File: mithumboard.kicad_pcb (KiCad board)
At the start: 2 copper layers, 28 parts, among them J1 AudioJack4, J2 AudioJack4, J3 AudioJack4, J4 AudioJack4, SW1 SW_Push, SW10 SW_Push, SW11 SW_Push, SW12 SW_Push, SW13 SW_Push, SW14 SW_Push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

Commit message: キースイッチのピン割り当て見直し
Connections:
- U1 pad 10: R2C2 -> R1C1
- U1 pad 11: R2C3 -> R1C2
- U1 pad 13: R2C4 -> R1C3
- U1 pad 14: R2C5 -> R1C4
- U1 pad 15: R3C1 -> R1C5
- U1 pad 16: R3C2 -> R2C4
- U1 pad 17: R3C3 -> R2C5
- U1 pad 18: R3C4 -> R3C5
- U1 pad 19: R3C5 -> R3C4
- U1 pad 4: R1C1 -> R3C3
- U1 pad 5: R1C2 -> R3C2
- U1 pad 6: R1C3 -> R3C1
- U1 pad 7: R1C4 -> R2C1
- U1 pad 8: R1C5 -> R2C3
- U1 pad 9: R2C1 -> R2C2
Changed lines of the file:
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@@
       (net 26 "Net-(U1-Pad20)"))
     (pad 19 smd rect (at 2.85 0.325) (size 1.1 0.4) (layers B.Cu B.Paste B.Mask)
+      (net 22 R3C4))
+    (pad 18 smd rect (at 2.85 -0.325) (size 1.1 0.4) (layers B.Cu B.Paste B.Mask)
       (net 23 R3C5))
-    (pad 18 smd rect (at 2.85 -0.325) (size 1.1 0.4) (layers B.Cu B.Paste B.Mask)
-      (net 22 R3C4))
     (pad 17 smd rect (at 2.85 -0.975) (size 1.1 0.4) (layers B.Cu B.Paste B.Mask)
-      (net 21 R3C3))
+      (net 18 R2C5))
     (pad 16 smd rect (at 2.85 -1.625) (size 1.1 0.4) (layers B.Cu B.Paste B.Mask)
-      (net 20 R3C2))
+      (net 17 R2C4))
     (pad 15 smd rect (at 2.85 -2.275) (size 1.1 0.4) (layers B.Cu B.Paste B.Mask)
-      (net 19 R3C1))
+      (net 13 R1C5))
     (pad 14 smd rect (at 2.85 -2.925) (size 1.1 0.4) (layers B.Cu B.Paste B.Mask)
-      (net 18 R2C5))
+      (net 12 R1C4))
     (pad 13 smd rect (at 2.85 -3.575) (size 1.1 0.4) (layers B.Cu B.Paste B.Mask)
-      (net 17 R2C4))
+      (net 11 R1C3))
     (pad 12 smd rect (at -2.85 -3.575) (size 1.1 0.4) (layers B.Cu B.Paste B.Mask)
       (net 1 GND))
     (pad 11 smd rect (at -2.85 -2.925) (size 1.1 0.4) (layers B.Cu B.Paste B.Mask)
+      (net 10 R1C2))
+    (pad 10 smd rect (at -2.85 -2.275) (size 1.1 0.4) (layers B.Cu B.Paste B.Mask)
+      (net 9 R1C1))
+    (pad 9 smd rect (at -2.85 -1.625) (size 1.1 0.4) (layers B.Cu B.Paste B.Mask)
+      (net 15 R2C2))
+    (pad 8 smd rect (at -2.85 -0.975) (size 1.1 0.4) (layers B.Cu B.Paste B.Mask)
       (net 16 R2C3))
-    (pad 10 smd rect (at -2.85 -2.275) (size 1.1 0.4) (layers B.Cu B.Paste B.Mask)
-      (net 15 R2C2))
-    (pad 9 smd rect (at -2.85 -1.625) (size 1.1 0.4) (layers B.Cu B.Paste B.Mask)
+    (pad 7 smd rect (at -2.85 -0.325) (size 1.1 0.4) (layers B.Cu B.Paste B.Mask)
       (net 14 R2C1))
-    (pad 8 smd rect (at -2.85 -0.975) (size 1.1 0.4) (layers B.Cu B.Paste B.Mask)
-      (net 13 R1C5))
-    (pad 7 smd rect (at -2.85 -0.325) (size 1.1 0.4) (layers B.Cu B.Paste B.Mask)
-      (net 12 R1C4))
     (pad 6 smd rect (at -2.85 0.325) (size 1.1 0.4) (layers B.Cu B.Paste B.Mask)
-      (net 11 R1C3))
+      (net 19 R3C1))
     (pad 5 smd rect (at -2.85 0.975) (size 1.1 0.4) (layers B.Cu B.Paste B.Mask)
-      (net 10 R1C2))
+      (net 20 R3C2))
     (pad 4 smd rect (at -2.85 1.625) (size 1.1 0.4) (layers B.Cu B.Paste B.Mask)
-      (net 9 R1C1))
+      (net 21 R3C3))
     (pad 3 smd rect (at -2.85 2.275) (size 1.1 0.4) (layers B.Cu B.Paste B.Mask)
       (net 8 A2))

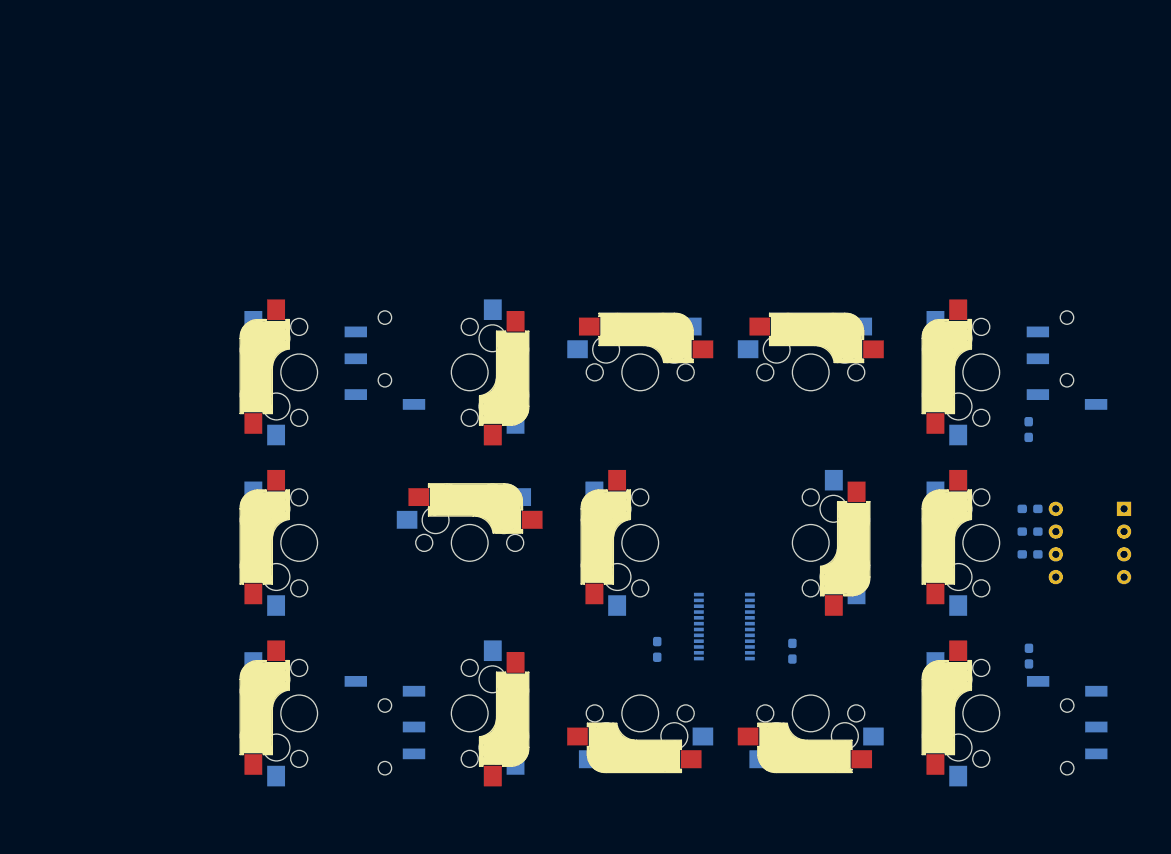
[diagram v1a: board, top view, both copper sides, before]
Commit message: 全部線引き終わり
ただし基板を180度回転させたので、キースイッチの行列のラベルを張りなおす必要あり。
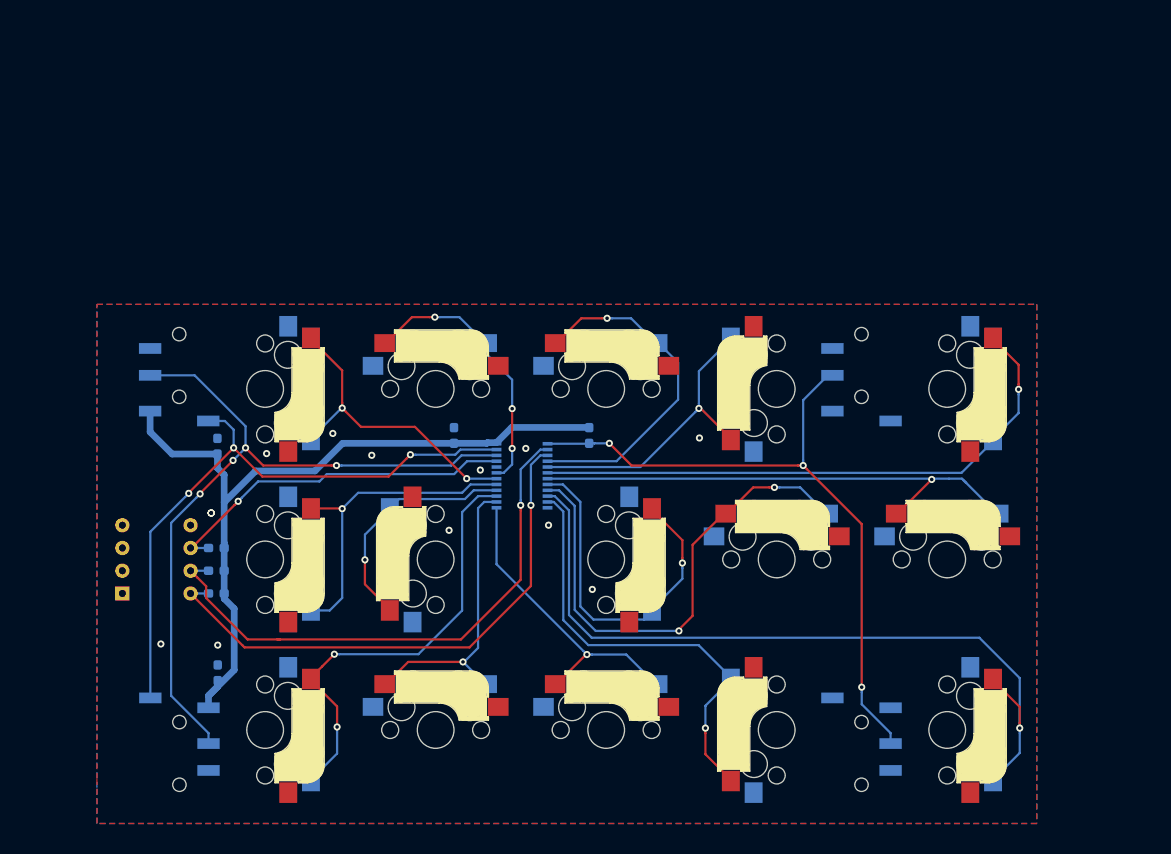
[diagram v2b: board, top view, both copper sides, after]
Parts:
- moved SW16 112.3 mm to (54.8, 104.3), turned to 0 degrees
- moved J1 107.9 mm to (61.2, 120.9), turned to 90 degrees
- moved J2 106.6 mm to (61.2, 80.1), turned to 270 degrees
- moved C3 94.6 mm to (65.5, 113.2), turned to 90 degrees
- moved C2 93.6 mm to (65.5, 87.9), turned to 90 degrees
- moved R1 91.4 mm to (65.3, 104.3), turned to 0 degrees
- moved R2 91.0 mm to (65.3, 101.8), turned to 0 degrees
- moved R3 90.9 mm to (65.3, 99.2), turned to 0 degrees
- moved SW13 89.4 mm to (70.8, 119.5), turned to 270 degrees
- moved SW15 87.8 mm to (70.8, 81.5), turned to 270 degrees
- moved SW1 82.7 mm to (147.0, 119.5), turned to 270 degrees
- moved SW3 81.0 mm to (147.0, 81.5), turned to 270 degrees
- moved SW14 80.0 mm to (70.8, 100.5), turned to 270 degrees
- moved SW2 72.4 mm to (147.0, 100.5), turned to 0 degrees
- moved J3 68.2 mm to (137.4, 120.9), turned to 90 degrees
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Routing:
- net 3.3V: track 0.00 -> 87.5 mm
- net R1C1: track 0.00 -> 87.5 mm, vias 0 -> 1
- net SCL: track 0.00 -> 83.0 mm, vias 0 -> 4
- net INT: track 0.00 -> 76.4 mm, vias 0 -> 3
- net SDA: track 0.00 -> 69.0 mm, vias 0 -> 3
- net R3C1: track 0.00 -> 65.1 mm, vias 0 -> 1
- net A1: track 0.00 -> 62.1 mm, vias 0 -> 1
- net A2: track 0.00 -> 61.2 mm, vias 0 -> 1
- net R2C1: track 0.00 -> 58.0 mm, vias 0 -> 1
- net R2C2: track 0.00 -> 57.2 mm, vias 0 -> 2
- net R1C2: track 0.00 -> 49.9 mm, vias 0 -> 1
- net R1C5: track 0.00 -> 49.5 mm, vias 0 -> 2
- net A0: track 0.00 -> 40.2 mm, vias 0 -> 1
- net R2C3: track 0.00 -> 39.5 mm, vias 0 -> 1
- net R3C3: track 0.00 -> 38.5 mm, vias 0 -> 1
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- added copper zone on B.Cu, net GND
- added copper zone on F.Cu, net GND

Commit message: ソケットのフットプリントを片面のみにし、再配線
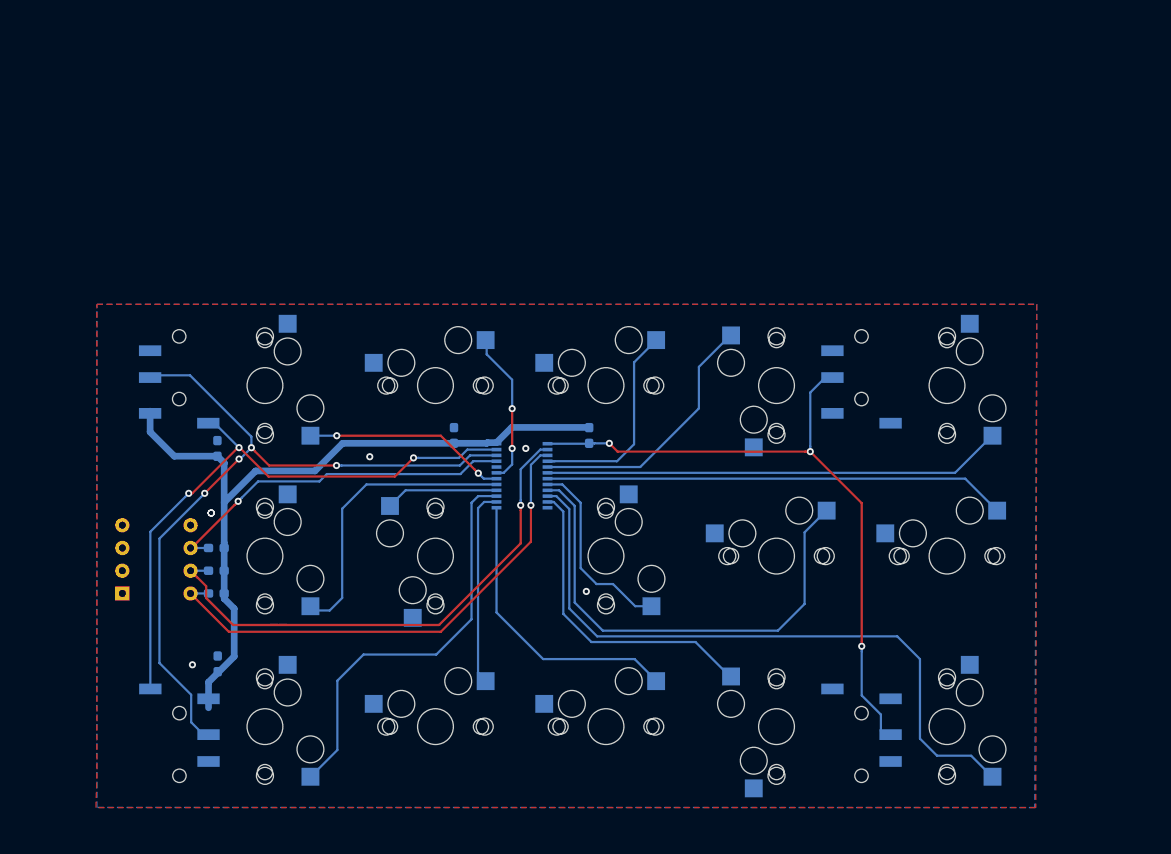
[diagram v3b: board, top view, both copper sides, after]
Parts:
- SW1, SW10, SW11, SW12, SW13, SW14, SW15, SW2, SW3, SW4, SW5, SW6, SW7, SW8, SW9: footprint kbd:CherryMX_Hotswap -> kbd:CherryMX_Hotswap_1side
- moved C3 1.00 mm to (65.5, 112.2)
- moved J1 1.00 mm to (61.2, 119.9)
- moved J3 1.00 mm to (137.4, 119.9)
- moved SW1 0.38 mm to (147.0, 119.2)
- moved SW2 0.38 mm to (147.0, 100.1)
- moved SW3 0.38 mm to (147.0, 81.1)
- moved SW10 0.38 mm to (89.8, 119.2)
- moved SW11 0.38 mm to (89.8, 100.1)
- moved SW12 0.38 mm to (89.8, 81.1)
- moved SW13 0.38 mm to (70.8, 119.2)
- moved SW14 0.38 mm to (70.8, 100.1)
- moved SW15 0.38 mm to (70.8, 81.1)
- moved SW4 0.38 mm to (127.9, 119.2)
- moved SW5 0.38 mm to (127.9, 100.1)
- moved SW6 0.38 mm to (127.9, 81.1)
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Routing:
- net R2C3: track 39.5 -> 21.5 mm, vias 1 -> 0
- net R3C3: track 38.5 -> 24.2 mm, vias 1 -> 0
- net R1C2: track 49.9 -> 35.9 mm, vias 1 -> 0
- net R3C1: track 65.1 -> 51.4 mm, vias 1 -> 0
- net R3C4: track 30.7 -> 17.0 mm, vias 3 -> 2
- net R2C4: track 26.5 -> 12.9 mm, vias 1 -> 0
- net R1C1: track 87.5 -> 74.6 mm, vias 1 -> 0
- net R3C5: track 34.9 -> 22.9 mm
- net R1C4: track 33.8 -> 22.1 mm, vias 1 -> 0
- net R2C1: track 58.0 -> 51.9 mm, vias 1 -> 0
- net R3C2: track 34.1 -> 29.2 mm, vias 1 -> 0
- net A2: track 61.2 -> 56.9 mm
- net R2C5: track 35.9 -> 32.4 mm, vias 1 -> 0
- net R1C5: track 49.5 -> 46.1 mm, vias 2 -> 0
- net R2C2: track 57.2 -> 54.4 mm, vias 2 -> 0
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
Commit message: さらに配線見直し。
配線は完了？
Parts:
- moved SW1 85.2 mm to (70.8, 81.1)
- moved SW13 85.2 mm to (147.0, 81.1)
- moved SW15 85.2 mm to (147.0, 119.2)
- moved SW3 85.2 mm to (70.8, 119.2)
- moved SW14 76.2 mm to (147.0, 100.1), turned to 0 degrees
- moved SW2 76.2 mm to (70.8, 100.1), turned to 270 degrees
- moved SW10 53.9 mm to (127.9, 81.1), turned to 90 degrees
- moved SW12 53.9 mm to (127.9, 119.2), turned to 90 degrees
- moved SW4 53.9 mm to (89.8, 81.1), turned to 0 degrees
- moved SW6 53.9 mm to (89.8, 119.2), turned to 0 degrees
- moved SW11 38.1 mm to (127.9, 100.1), turned to 0 degrees
- moved SW5 38.1 mm to (89.8, 100.1), turned to 90 degrees
- moved SW7 38.1 mm to (108.9, 81.1)
- moved SW9 38.1 mm to (108.9, 119.2)
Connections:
- SW11 pad 1: GND -> R2C4
- SW11 pad 2: R2C4 -> GND
- SW15 pad 1: GND -> R3C5
- SW15 pad 2: R3C5 -> GND
- SW2 pad 1: GND -> R2C1
- SW2 pad 2: R2C1 -> GND
- SW3 pad 1: GND -> R3C1
- SW3 pad 2: R3C1 -> GND
- SW8 pad 1: GND -> R2C3
- SW8 pad 2: R2C3 -> GND
- SW9 pad 1: GND -> R3C3
- SW9 pad 2: R3C3 -> GND
- U1 pad 10: R1C1 -> R3C5
- U1 pad 11: R1C2 -> R3C4
- U1 pad 13: R1C3 -> R3C3
- U1 pad 14: R1C4 -> R3C2
- U1 pad 15: R1C5 -> R3C1
- U1 pad 16: R2C4 -> R2C2
- U1 pad 17: R2C5 -> R2C1
- U1 pad 18: R3C5 -> R1C1
- U1 pad 19: R3C4 -> R1C2
- U1 pad 4: R3C3 -> R1C3
- U1 pad 5: R3C2 -> R1C4
- U1 pad 6: R3C1 -> R1C5
- U1 pad 7: R2C1 -> R2C5
- U1 pad 9: R2C2 -> R2C4
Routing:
- net R1C1: track 74.6 -> 22.9 mm, vias 0 -> 2
- net R2C2: track 54.4 -> 12.9 mm
- net R3C5: track 22.9 -> 61.6 mm, vias 2 -> 0
- net R2C1: track 51.9 -> 23.8 mm
- net R3C1: track 51.4 -> 31.1 mm
- net R2C5: track 32.4 -> 51.9 mm
- net R3C4: track 17.0 -> 35.9 mm, vias 2 -> 0
- net R1C2: track 35.9 -> 17.0 mm, vias 0 -> 2
- net R2C3: track 21.5 -> 9.53 mm
- net R1C3: track 33.1 -> 24.2 mm
- net R2C4: track 12.9 -> 21.3 mm
- net R3C2: track 29.2 -> 22.1 mm
- net R1C4: track 22.1 -> 29.2 mm
- net R1C5: track 46.1 -> 51.4 mm
- net 3.3V: track 85.3 -> 84.3 mm
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
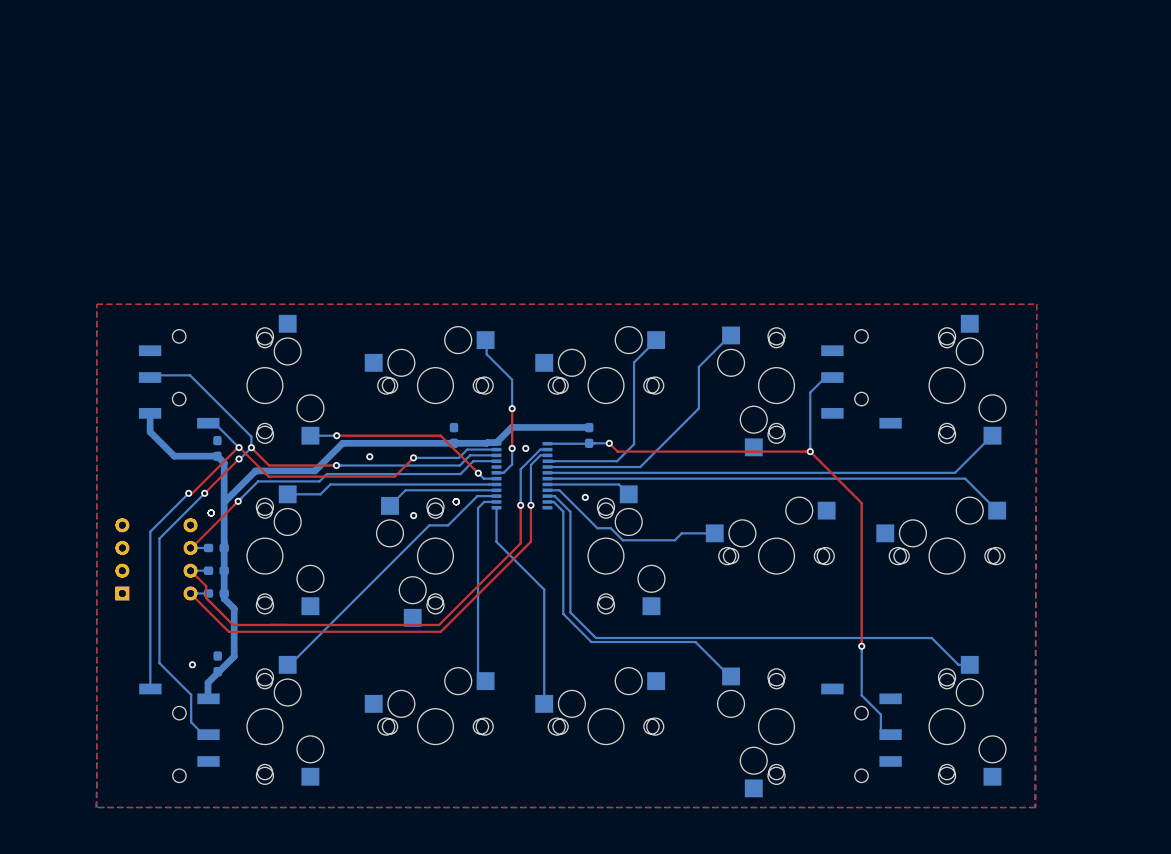
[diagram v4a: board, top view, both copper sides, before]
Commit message: PJ-320D のピンアサインを修正して、配線・配置を再整頓
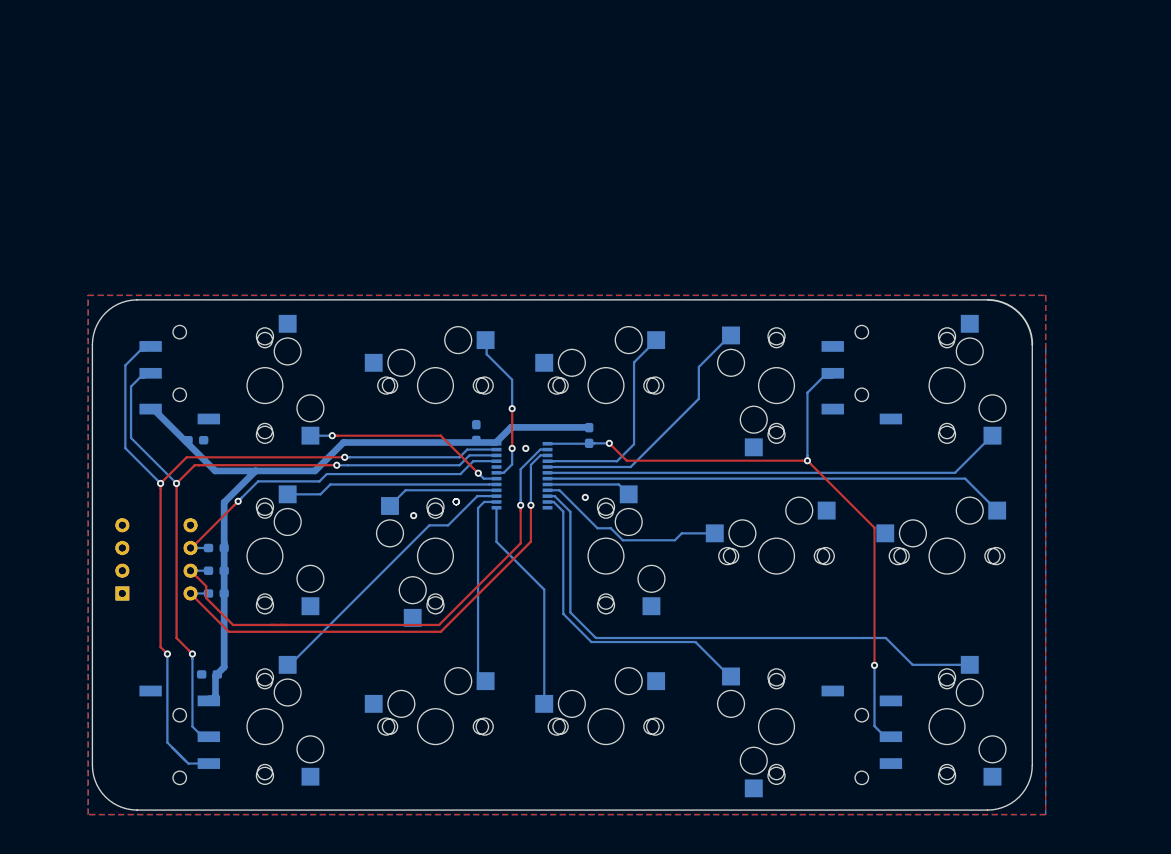
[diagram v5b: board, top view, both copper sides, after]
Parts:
- J1, J2, J3, J4: footprint Connector_Audio:Jack_3.5mm_PJ320D_Horizontal -> Connector_Audio_Mod:Jack_3.5mm_PJ320D_Horizontal_Mod
- moved J1 40.0 mm to (61.3, 79.9), turned to 270 degrees
- moved J3 40.0 mm to (137.5, 79.9), turned to 270 degrees
- moved J2 39.8 mm to (61.3, 120.1), turned to 90 degrees
- moved J4 39.8 mm to (137.5, 120.1), turned to 90 degrees
- moved C2 2.58 mm to (63.1, 87.2), turned to 0 degrees
- moved C1 2.52 mm to (94.4, 86.3)
- moved C3 1.50 mm to (64.6, 113.3), turned to 180 degrees
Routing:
- net SDA: track 67.6 -> 93.8 mm
- net 3.3V: track 84.3 -> 81.8 mm
- net INT: track 74.2 -> 75.9 mm
- net SCL: track 83.0 -> 82.0 mm, vias 4 -> 3
- net R1C4: track 29.2 -> 28.5 mm
- net GND: vias 11 -> 6
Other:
- board outline added: 105 x 57 mm

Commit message: スペーサー用の穴をあけるのを忘れてた
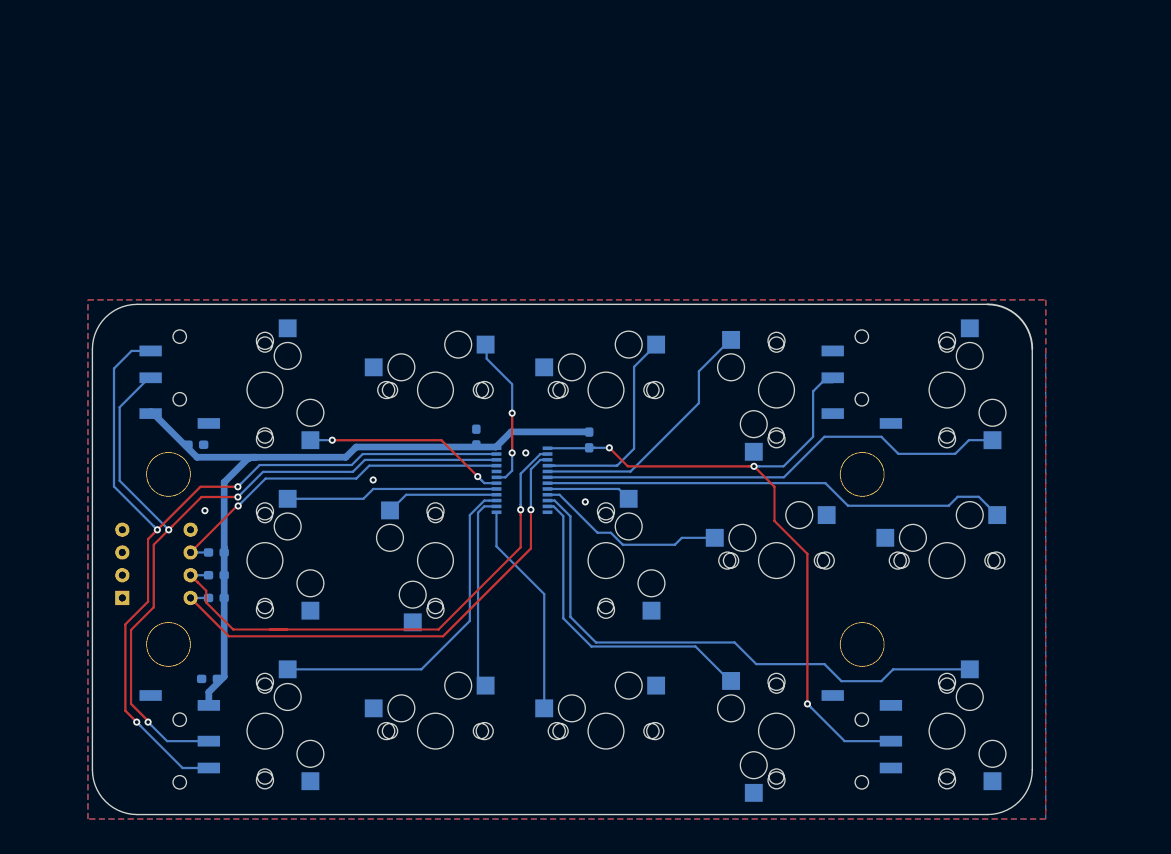
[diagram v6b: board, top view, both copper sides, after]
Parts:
- added Ref**: Val**, kbd:HOLE, F.Cu at (137.5, 91.0)
- added Ref**: Val**, kbd:HOLE, F.Cu at (137.5, 110.0)
- added Ref**: Val**, kbd:HOLE, F.Cu at (60.0, 91.0)
- added Ref**: Val**, kbd:HOLE, F.Cu at (60.0, 110.0)
- moved C1 0.50 mm to (94.4, 86.8)
- moved C2 0.50 mm to (63.1, 87.7)
- moved C3 0.50 mm to (64.6, 113.8)
- moved J1 0.50 mm to (61.3, 80.4)
- moved J2 0.50 mm to (61.3, 120.6)
- moved J3 0.50 mm to (137.5, 80.4)
- moved J4 0.50 mm to (137.5, 120.6)
- moved R1 0.50 mm to (65.3, 104.8)
- moved R2 0.50 mm to (65.3, 102.3)
- moved R3 0.50 mm to (65.3, 99.7)
- moved R4 0.50 mm to (107.0, 87.2)
- moved SW1 0.50 mm to (70.8, 81.6)
- moved SW10 0.50 mm to (127.9, 81.6)
- moved SW11 0.50 mm to (127.9, 100.6)
- moved SW12 0.50 mm to (127.9, 119.7)
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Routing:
- net SCL: track 82.0 -> 91.6 mm
- net R3C1: track 31.1 -> 38.1 mm
- net SDA: track 93.8 -> 100.0 mm
- net INT: track 75.9 -> 81.0 mm
- net R1C5: track 51.4 -> 53.2 mm
- net R3C5: track 61.6 -> 62.7 mm
- net R2C5: track 51.9 -> 52.8 mm
- net 3.3V: track 81.8 -> 82.3 mm
- net GND: vias 6 -> 4
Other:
- board text added: "mithumboard Designed by mitaroThanken"
